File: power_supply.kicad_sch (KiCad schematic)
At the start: 59 parts, among them Q1201 NX7002AK, Q1202 PMN48XP, U1201 TL431PK, U1202 TL431PK, U1203 TL431PK, U1204 MCP1825T-330, U1205 NCV8164ASN120T1G, U1206 MCP1825T-330, U1207 NCV8164ASN250T1G, U1208 NCV8164ASN330T1G

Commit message: Combined update (kicad 6.0.4..) - Update schematic to kicad 6.0.4 - Assign footprints for SMA connectors - Replace MCP1825T with MCP1824T (chip shortages..)
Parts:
- U1204, U1206: value MCP1825T-330 -> MCP1824T-330; Mfr PN MCP1825T-3302E/DC -> MCP1824T-3302E/DC
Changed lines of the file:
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@@
     (in_bom yes) (on_board yes) (fields_autoplaced)
     (property "Reference" "U1206" (id 0) (at 208.28 70.5952 0))
-    (property "Value" "MCP1825T-330" (id 1) (at 208.28 73.1321 0))
+    (property "Value" "MCP1824T-330" (id 1) (at 208.28 73.1321 0))
     (property "Footprint" "Package_TO_SOT_SMD:SOT-223-6" (id 2) (at 203.2 72.39 0)
       (effects (font (size 1.27 1.27)) hide)
@@
       (effects (font (size 1.27 1.27)) hide)
     )
-    (property "Mfr PN" "MCP1825T-3302E/DC" (id 5) (at 208.28 76.2 0)
+    (property "Mfr PN" "MCP1824T-3302E/DC" (id 5) (at 208.28 76.2 0)
       (effects (font (size 1.27 1.27)) hide)
     )
@@
     (in_bom yes) (on_board yes) (fields_autoplaced)
     (property "Reference" "U1204" (id 0) (at 104.14 19.7952 0))
-    (property "Value" "MCP1825T-330" (id 1) (at 104.14 22.3321 0))
+    (property "Value" "MCP1824T-330" (id 1) (at 104.14 22.3321 0))
     (property "Footprint" "Package_TO_SOT_SMD:SOT-223-6" (id 2) (at 99.06 21.59 0)
       (effects (font (size 1.27 1.27)) hide)
@@
       (effects (font (size 1.27 1.27)) hide)
     )
-    (property "Mfr PN" "MCP1825T-3302E/DC" (id 5) (at 104.14 25.4 0)
-      (effects (font (size 1.27 1.27)) hide)
-    )
+    (property "Mfr PN" "MCP1824T-3302E/DC" (id 5) (at 104.14 25.4 0)
+      (effects (font (size 1.27 1.27)) hide)
+    )

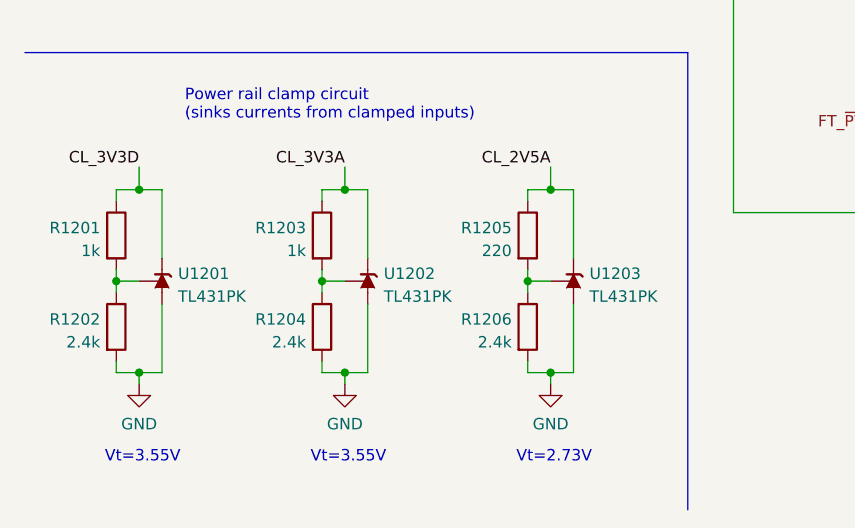
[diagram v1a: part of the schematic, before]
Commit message: Replace TL431PK (sot89) with TL431AFDT (sot23)
- Fix tl431 value & footprint (kicad 6.0.4 bug)
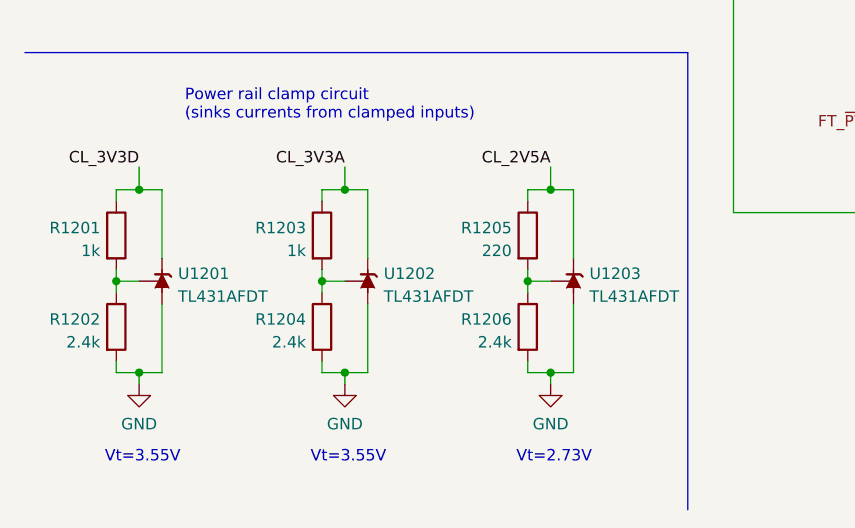
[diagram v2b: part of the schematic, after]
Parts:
- removed U1201, U1202, U1203: TL431PK, Package_TO_SOT_SMD:SOT-89-3, symbol Reference_Voltage:TL431PK
- added U1201, U1202, U1203: TL431AFDT, Package_TO_SOT_SMD:SOT-23, symbol Reference_Voltage:TL431DBZ
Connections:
- net GND: now also U1201.3 (A), U1202.3 (A), U1203.3 (A)
- net OUT_2V5A: now also U1203.1 (K)
- net OUT_3V3A: now also U1202.1 (K)
- net OUT_3V3D: now also U1201.1 (K)
- net at R1201.2, R1202.1: now also U1201.2 (REF)
- net at R1203.2, R1204.1: now also U1202.2 (REF)
- net at R1205.2, R1206.1: now also U1203.2 (REF)
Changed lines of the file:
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@@
     (pin "2")
-  )
-  (symbol (lib_id "Reference_Voltage:TL431PK") (at 53.34 165.1 90) (unit 1)
-    (in_bom yes) (on_board yes) (fields_autoplaced)
-    (property "Reference" "U1202" (id 0) (at 55.118 164.2653 90)
-      (effects (font (size 1.27 1.27)) (justify right))
-    )
-    (property "Value" "TL431PK" (id 1) (at 55.118 166.8022 90)
-      (effects (font (size 1.27 1.27)) (justify right))
-    )
-    (property "Footprint" "Package_TO_SOT_SMD:SOT-89-3" (id 2) (at 57.15 165.1 0)
-      (effects (font (size 1.27 1.27) italic) hide)
-    )
-    (property "Datasheet" "http://www.ti.com/lit/ds/symlink/tl431.pdf" (id 3) (at 53.34 165.1 0)
-      (effects (font (size 1.27 1.27) italic) hide)
-    )
-    (property "Mfr" "Texas Instruments" (id 4) (at 53.34 165.1 0)
-      (effects (font (size 1.27 1.27)) hide)
-    )
-    (property "Mfr PN" "TL431ACPK" (id 5) (at 53.34 165.1 0)
-      (effects (font (size 1.27 1.27)) hide)
-    )
-    (pin "1")
-    (pin "2")
-    (pin "3")
   )
   (symbol (lib_id "power:GND") (at 67.31 87.63 0) (unit 1)
@@
     (pin "2")
   )
+  (symbol (lib_id "Reference_Voltage:TL431DBZ") (at 53.34 165.1 90) (unit 1)
+    (in_bom yes) (on_board yes) (fields_autoplaced)
+    (property "Reference" "U1202" (id 0) (at 55.118 164.2653 90)
+      (effects (font (size 1.27 1.27)) (justify right))
+    )
+    (property "Value" "TL431AFDT" (id 1) (at 55.118 166.8022 90)
+      (effects (font (size 1.27 1.27)) (justify right))
+    )
+    (property "Footprint" "Package_TO_SOT_SMD:SOT-23" (id 2) (at 57.15 165.1 0)
+      (effects (font (size 1.27 1.27) italic) hide)
+    )
+    (property "Datasheet" "https://assets.nexperia.com/documents/data-sheet/TL431_FAM.pdf" (id 3) (at 53.34 165.1 0)
+      (effects (font (size 1.27 1.27) italic) hide)
+    )
+    (property "Mfr" "Nexperia" (id 4) (at 53.34 165.1 0)
+      (effects (font (size 1.27 1.27)) hide)
+    )
+    (property "Mfr PN" "TL431AFDT,215" (id 5) (at 53.34 165.1 0)
+      (effects (font (size 1.27 1.27)) hide)
+    )
+    (pin "1")
+    (pin "2")
+    (pin "3")
+  )
   (symbol (lib_id "Device:R") (at 134.62 120.65 0) (unit 1)
     (in_bom yes) (on_board yes) (fields_autoplaced)
@@
     (pin "1")
     (pin "2")
-  )
-  (symbol (lib_id "Reference_Voltage:TL431PK") (at 76.2 165.1 90) (unit 1)
-    (in_bom yes) (on_board yes) (fields_autoplaced)
-    (property "Reference" "U1203" (id 0) (at 77.978 164.2653 90)
-      (effects (font (size 1.27 1.27)) (justify right))
-    )
-    (property "Value" "TL431PK" (id 1) (at 77.978 166.8022 90)
-      (effects (font (size 1.27 1.27)) (justify right))
-    )
-    (property "Footprint" "Package_TO_SOT_SMD:SOT-89-3" (id 2) (at 80.01 165.1 0)
-      (effects (font (size 1.27 1.27) italic) hide)
-    )
-    (property "Datasheet" "http://www.ti.com/lit/ds/symlink/tl431.pdf" (id 3) (at 76.2 165.1 0)
-      (effects (font (size 1.27 1.27) italic) hide)
-    )
-    (property "Mfr" "Texas Instruments" (id 4) (at 76.2 165.1 0)
-      (effects (font (size 1.27 1.27)) hide)
-    )
-    (property "Mfr PN" "TL431ACPK" (id 5) (at 76.2 165.1 0)
-      (effects (font (size 1.27 1.27)) hide)
-    )
-    (pin "1")
-    (pin "2")
-    (pin "3")
   )
   (symbol (lib_id "power:GND") (at 228.6 115.57 0) (unit 1)
@@
     (pin "1")
   )
+  (symbol (lib_id "Reference_Voltage:TL431DBZ") (at 30.48 165.1 90) (unit 1)
+    (in_bom yes) (on_board yes) (fields_autoplaced)
+    (property "Reference" "U1201" (id 0) (at 32.258 164.2653 90)
+      (effects (font (size 1.27 1.27)) (justify right))
+    )
+    (property "Value" "TL431AFDT" (id 1) (at 32.258 166.8022 90)
+      (effects (font (size 1.27 1.27)) (justify right))
+    )
+    (property "Footprint" "Package_TO_SOT_SMD:SOT-23" (id 2) (at 34.29 165.1 0)
+      (effects (font (size 1.27 1.27) italic) hide)
+    )
+    (property "Datasheet" "https://assets.nexperia.com/documents/data-sheet/TL431_FAM.pdf" (id 3) (at 30.48 165.1 0)
+      (effects (font (size 1.27 1.27) italic) hide)
+    )
+    (property "Mfr" "Nexperia" (id 4) (at 30.48 165.1 0)
+      (effects (font (size 1.27 1.27)) hide)
+    )
+    (property "Mfr PN" "TL431AFDT,215" (id 5) (at 30.48 165.1 0)
+      (effects (font (size 1.27 1.27)) hide)
+    )
+    (pin "1")
+    (pin "2")
+    (pin "3")
+  )
   (symbol (lib_id "Device:R") (at 71.12 160.02 0) (unit 1)
     (in_bom yes) (on_board yes) (fields_autoplaced)
@@
     (pin "2")
   )
+  (symbol (lib_id "Reference_Voltage:TL431DBZ") (at 76.2 165.1 90) (unit 1)
+    (in_bom yes) (on_board yes) (fields_autoplaced)
+    (property "Reference" "U1203" (id 0) (at 77.978 164.2653 90)
+      (effects (font (size 1.27 1.27)) (justify right))
+    )
+    (property "Value" "TL431AFDT" (id 1) (at 77.978 166.8022 90)
+      (effects (font (size 1.27 1.27)) (justify right))
+    )
+    (property "Footprint" "Package_TO_SOT_SMD:SOT-23" (id 2) (at 80.01 165.1 0)
+      (effects (font (size 1.27 1.27) italic) hide)
+    )
+    (property "Datasheet" "https://assets.nexperia.com/documents/data-sheet/TL431_FAM.pdf" (id 3) (at 76.2 165.1 0)
+      (effects (font (size 1.27 1.27) italic) hide)
+    )
+    (property "Mfr" "Nexperia" (id 4) (at 76.2 165.1 0)
+      (effects (font (size 1.27 1.27)) hide)
+    )
+    (property "Mfr PN" "TL431AFDT,215" (id 5) (at 76.2 165.1 0)
+      (effects (font (size 1.27 1.27)) hide)
+    )
+    (pin "1")
+    (pin "2")
+    (pin "3")
+  )
   (symbol (lib_id "Device:C") (at 129.54 31.75 0) (unit 1)
     (in_bom yes) (on_board yes) (fields_autoplaced)
@@
     (pin "1")
   )
-  (symbol (lib_id "Reference_Voltage:TL431PK") (at 30.48 165.1 90) (unit 1)
-    (in_bom yes) (on_board yes) (fields_autoplaced)
-    (property "Reference" "U1201" (id 0) (at 32.258 164.2653 90)
-      (effects (font (size 1.27 1.27)) (justify right))
-    )
-    (property "Value" "TL431PK" (id 1) (at 32.258 166.8022 90)
-      (effects (font (size 1.27 1.27)) (justify right))
-    )
-    (property "Footprint" "Package_TO_SOT_SMD:SOT-89-3" (id 2) (at 34.29 165.1 0)
-      (effects (font (size 1.27 1.27) italic) hide)
-    )
-    (property "Datasheet" "http://www.ti.com/lit/ds/symlink/tl431.pdf" (id 3) (at 30.48 165.1 0)
-      (effects (font (size 1.27 1.27) italic) hide)
-    )
-    (property "Mfr" "Texas Instruments" (id 4) (at 30.48 165.1 0)
-      (effects (font (size 1.27 1.27)) hide)
-    )
-    (property "Mfr PN" "TL431ACPK" (id 5) (at 30.48 165.1 0)
-      (effects (font (size 1.27 1.27)) hide)
-    )
-    (pin "1")
-    (pin "2")
-    (pin "3")
-  )
   (symbol (lib_id "Device:C") (at 85.09 31.75 0) (unit 1)

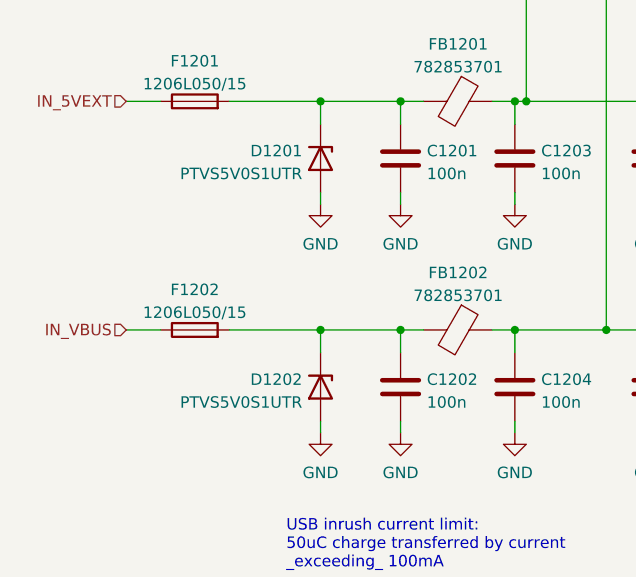
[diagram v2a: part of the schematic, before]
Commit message: PN list: replace PTVSxxS1UTR with PTVSxxS1UR
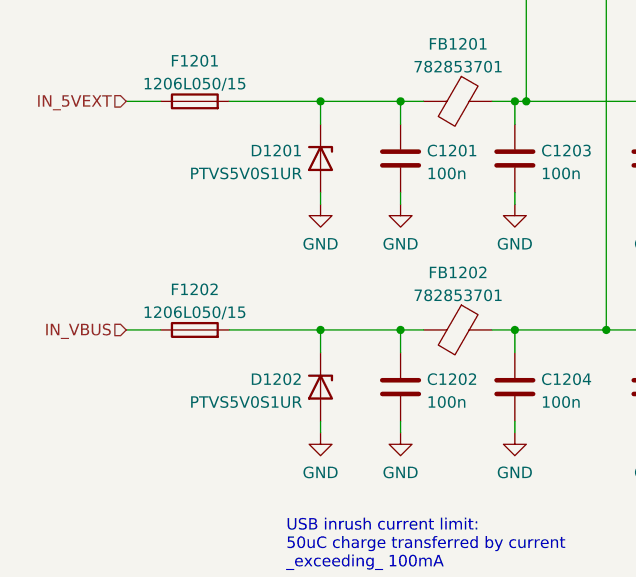
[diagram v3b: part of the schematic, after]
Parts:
- D1201, D1202: value PTVS5V0S1UTR -> PTVS5V0S1UR; Mfr PN PTVS5V0S1UTR,115 -> PTVS5V0S1UR,115
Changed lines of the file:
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@@
       (effects (font (size 1.27 1.27)) (justify right))
     )
-    (property "Value" "PTVS5V0S1UTR" (id 1) (at 43.6881 84.2522 90)
+    (property "Value" "PTVS5V0S1UR" (id 1) (at 43.6881 84.2522 90)
       (effects (font (size 1.27 1.27)) (justify right))
     )
@@
       (effects (font (size 1.27 1.27)) hide)
     )
-    (property "Mfr PN" "PTVS5V0S1UTR,115 " (id 5) (at 45.72 82.55 0)
+    (property "Mfr PN" "PTVS5V0S1UR,115" (id 5) (at 45.72 82.55 0)
       (effects (font (size 1.27 1.27)) hide)
     )
@@
       (effects (font (size 1.27 1.27)) (justify right))
     )
-    (property "Value" "PTVS5V0S1UTR" (id 1) (at 43.6881 109.6522 90)
+    (property "Value" "PTVS5V0S1UR" (id 1) (at 43.6881 109.6522 90)
       (effects (font (size 1.27 1.27)) (justify right))
     )
@@
       (effects (font (size 1.27 1.27)) hide)
     )
-    (property "Mfr PN" "PTVS5V0S1UTR,115 " (id 5) (at 45.72 107.95 0)
+    (property "Mfr PN" "PTVS5V0S1UR,115" (id 5) (at 45.72 107.95 0)
       (effects (font (size 1.27 1.27)) hide)
     )

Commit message: Update footprints: - SOD323F, SOD323, SOD123W... intead of generic handsolder version - 3225 xtal - use handsolder footprint - do not use handsolder version for ferrite beads - use SOT-23-6 instead of TSOP-6
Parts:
- D1201, D1202, D1205: footprint Diode_SMD:D_SOD-123 -> Diode_SMD:Nexperia_CFP3_SOD-123W
- D1203, D1204, D1206, D1207: footprint Diode_SMD:D_SOD-123 -> Diode_SMD:D_SOD-123F
- FB1201, FB1202: footprint Inductor_SMD:L_0805_2012Metric_Pad1.05x1.20mm_HandSolder -> Inductor_SMD:L_0805_2012Metric
- Q1202: footprint Package_SO:TSOP-6_1.65x3.05mm_P0.95mm -> Package_TO_SOT_SMD:SOT-23-6
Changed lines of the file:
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@@
     (property "Reference" "FB1201" (id 0) (at 61.0108 69.8586 90))
     (property "Value" "782853701" (id 1) (at 61.0108 72.3955 90))
-    (property "Footprint" "Inductor_SMD:L_0805_2012Metric_Pad1.05x1.20mm_HandSolder" (id 2) (at 60.96 74.422 90)
+    (property "Footprint" "Inductor_SMD:L_0805_2012Metric" (id 2) (at 60.96 74.422 90)
       (effects (font (size 1.27 1.27)) hide)
     )
@@
     (property "Reference" "FB1202" (id 0) (at 61.0108 95.2586 90))
     (property "Value" "782853701" (id 1) (at 61.0108 97.7955 90))
-    (property "Footprint" "Inductor_SMD:L_0805_2012Metric_Pad1.05x1.20mm_HandSolder" (id 2) (at 60.96 99.822 90)
+    (property "Footprint" "Inductor_SMD:L_0805_2012Metric" (id 2) (at 60.96 99.822 90)
       (effects (font (size 1.27 1.27)) hide)
     )
@@
     (property "Reference" "D1206" (id 0) (at 152.7175 71.2302 0))
     (property "Value" "SBR3U40S1F" (id 1) (at 152.7175 73.7671 0))
-    (property "Footprint" "Diode_SMD:D_SOD-123" (id 2) (at 152.4 76.2 0)
+    (property "Footprint" "Diode_SMD:D_SOD-123F" (id 2) (at 152.4 76.2 0)
       (effects (font (size 1.27 1.27)) hide)
     )
@@
       (effects (font (size 1.27 1.27)) (justify right))
     )
-    (property "Footprint" "Diode_SMD:D_SOD-123" (id 2) (at 68.58 50.8 0)
+    (property "Footprint" "Diode_SMD:D_SOD-123F" (id 2) (at 68.58 50.8 0)
       (effects (font (size 1.27 1.27)) hide)
     )
@@
     (property "Reference" "D1207" (id 0) (at 152.7175 96.6302 0))
     (property "Value" "SBR3U40S1F" (id 1) (at 152.7175 99.1671 0))
-    (property "Footprint" "Diode_SMD:D_SOD-123" (id 2) (at 152.4 101.6 0)
+    (property "Footprint" "Diode_SMD:D_SOD-123F" (id 2) (at 152.4 101.6 0)
       (effects (font (size 1.27 1.27)) hide)
     )
@@
       (effects (font (size 1.27 1.27)) (justify left))
     )
-    (property "Footprint" "Diode_SMD:D_SOD-123" (id 2) (at 77.47 50.8 0)
+    (property "Footprint" "Diode_SMD:D_SOD-123F" (id 2) (at 77.47 50.8 0)
       (effects (font (size 1.27 1.27)) hide)
     )
@@
       (effects (font (size 1.27 1.27)) (justify left))
     )
-    (property "Footprint" "Diode_SMD:D_SOD-123" (id 2) (at 142.24 31.75 0)
+    (property "Footprint" "Diode_SMD:Nexperia_CFP3_SOD-123W" (id 2) (at 142.24 31.75 0)
       (effects (font (size 1.27 1.27)) hide)
     )
@@
       (effects (font (size 1.27 1.27)) (justify right))
     )
-    (property "Footprint" "Diode_SMD:D_SOD-123" (id 2) (at 45.72 82.55 0)
+    (property "Footprint" "Diode_SMD:Nexperia_CFP3_SOD-123W" (id 2) (at 45.72 82.55 0)
       (effects (font (size 1.27 1.27)) hide)
     )
@@
     (property "Reference" "Q1202" (id 0) (at 133.35 95.9952 90))
     (property "Value" "PMN48XP" (id 1) (at 133.35 98.5321 90))
-    (property "Footprint" "Package_SO:TSOP-6_1.65x3.05mm_P0.95mm" (id 2) (at 130.81 99.06 0)
+    (property "Footprint" "Package_TO_SOT_SMD:SOT-23-6" (id 2) (at 130.81 99.06 0)
       (effects (font (size 1.27 1.27)) (justify left) hide)
     )
@@
       (effects (font (size 1.27 1.27)) (justify right))
     )
-    (property "Footprint" "Diode_SMD:D_SOD-123" (id 2) (at 45.72 107.95 0)
-      (effects (font (size 1.27 1.27)) hide)
-    )
+    (property "Footprint" "Diode_SMD:Nexperia_CFP3_SOD-123W" (id 2) (at 45.72 107.95 0)
+      (effects (font (size 1.27 1.27)) hide)
+    )

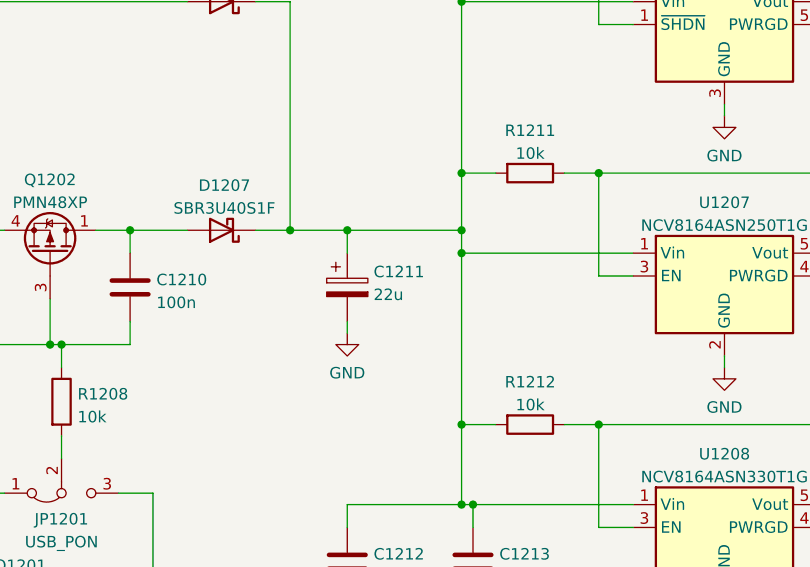
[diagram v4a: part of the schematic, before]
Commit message: Replace 10uf al-elco by tantalum -Space savings (0805 vs 4mm cylinder)
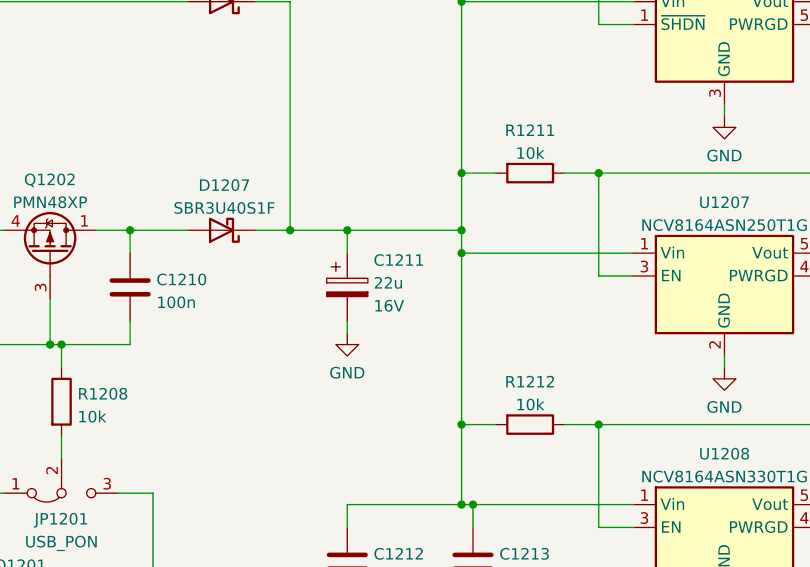
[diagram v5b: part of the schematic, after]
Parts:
- C1211: Spec1 (none) -> 16V
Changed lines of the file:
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@@
   (symbol (lib_id "Device:C_Polarized") (at 166.37 107.95 0) (unit 1)
     (in_bom yes) (on_board yes) (fields_autoplaced)
-    (property "Reference" "C1211" (id 0) (at 169.291 106.2263 0)
+    (property "Reference" "C1211" (id 0) (at 169.291 104.9579 0)
       (effects (font (size 1.27 1.27)) (justify left))
     )
-    (property "Value" "22u" (id 1) (at 169.291 108.7632 0)
+    (property "Value" "22u" (id 1) (at 169.291 107.4948 0)
       (effects (font (size 1.27 1.27)) (justify left))
     )
@@
       (effects (font (size 1.27 1.27)) hide)
     )
-    (property "Spec1" "" (id 4) (at 169.291 108.7632 0)
+    (property "Spec1" "16V" (id 4) (at 169.291 110.0317 0)
       (effects (font (size 1.27 1.27)) (justify left))
     )
-    (property "Spec2" "" (id 5) (at 169.291 111.3001 0)
-      (effects (font (size 1.27 1.27)) (justify left))
-    )
-    (property "Tolerance" "" (id 6) (at 166.37 107.95 0)
-      (effects (font (size 1.27 1.27)) hide)
-    )
     (property "Mfr" "Nichicon" (id 7) (at 166.37 107.95 0)
